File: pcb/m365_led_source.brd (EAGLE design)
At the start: 24 x 69 mm, 36 parts, among them M1 BSC037N08NS5ATMA1, M2 CSD19534Q5A

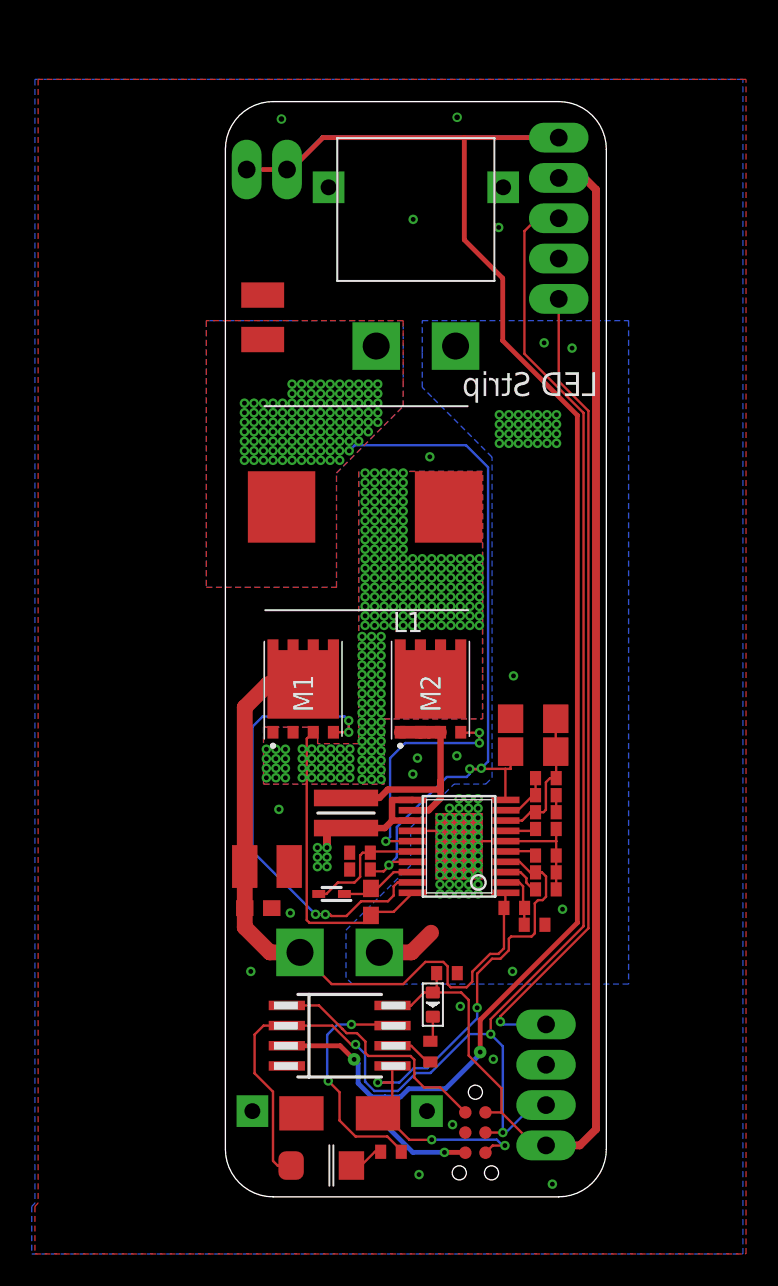
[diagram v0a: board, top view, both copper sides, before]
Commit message: Updated led source board. Added RTC chip + regulator for it Changed the pinout of the attiny45 so that it can be programmed in place
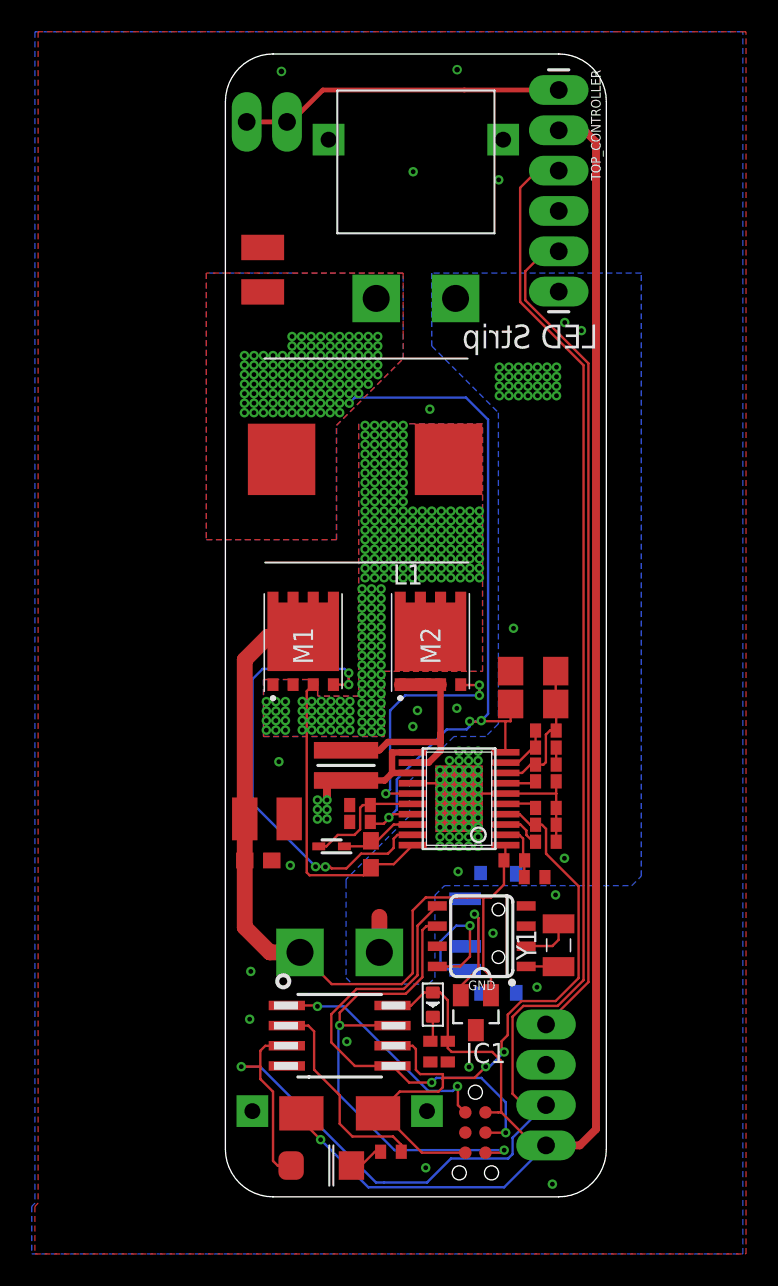
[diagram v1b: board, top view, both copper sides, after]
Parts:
- added GND: DS1307Z, SparkFun-Clocks:SO08-0.15
- added IC1: ZXTR2105FQ, linear:SOT23
- added U$2: MSK-12C02_SMD_SPDT_SWITCH, MSK-12C02 SMD Micro Slider Switch SPDT:MSK-12C02
- added Y1: SMD-3215_2P32.768KHZ12.5PF10PP, SMD-3215_2P32.768KHZ12.5PF10PP:SMD3215_2P32768KHZ125PF10PPM
- TOP_CONTROLLER: device SparkFun-Connectors:1X05_LONGPADS -> SparkFun-Connectors:1X06_LONGPADS
- moved C1 4.94 mm to (14.0, 9.15), turned to 270 degrees
- moved CIN 3.00 mm to (2.62, 23.8)
- moved CINX 3.00 mm to (2.07, 21.2)
- moved C_BOOT 3.00 mm to (9.17, 21.6)
- moved C_COMP 3.00 mm to (20.2, 28.3)
- moved C_COMP2 3.00 mm to (20.2, 29.4)
- moved C_OUT 3.00 mm to (2.35, 58.4)
- moved C_RAMP 3.00 mm to (20.2, 24.5)
- moved C_SS 3.00 mm to (20.2, 26.2)
- moved C_VCC 3.00 mm to (8.48, 24.7)
- moved C_VCCX 3.00 mm to (8.48, 23.6)
- moved D1 3.00 mm to (6.69, 22.1)
- moved L1 3.00 mm to (8.81, 46.5)
- moved LED 3.00 mm to (12.0, 56.6), turned to 270 degrees
- moved LED_DATA 3.00 mm to (3.88, 67.7)
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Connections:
- removed net EN: ATTINY85.5, J2.6, LM5116.4, R_EN_PULLDOWN.2, U$1.P$1
- new net 5V_REG: IC1.2, U$2.COM
- new net N$11: GND.2, Y1.2
- new net N$6: GND.1, Y1.1
- new net PB0: ATTINY85.5, GND.5, J2.4
- new net PB1: ATTINY85.6, J2.5, LM5116.4, R_EN_PULLDOWN.2, U$1.P$1
- new net PB3: ATTINY85.2, R_DATA.1
- net GND: now also GND.3, GND.4, IC1.3, R_LED.1, U$2.GND@1, U$2.GND@2, U$2.GND@3, U$2.GND@4; no longer U$1.P$2
- net M365_5V: now also U$1.P$2
- net M365_DATA: now also ATTINY85.3; no longer ATTINY85.2, J2.4
- net M365_LED_DATA: no longer ATTINY85.3, J2.5
- net N$3: now also GND.8, U$2.L1; no longer ATTINY85.6, R_LED.1
- net PB2: now also GND.6, J2.6; no longer R_DATA.1
- net VIN: now also IC1.1
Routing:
- net M365_LED_DATA: track 124.6 -> 20.5 mm, vias 3 -> 0
- net PB1: track 0.00 -> 42.8 mm, vias 0 -> 2
- net EN: track 38.1 -> 0.00 mm, vias 4 -> 0
- net PB0: track 0.00 -> 29.1 mm, vias 0 -> 2
- net M365_5V: track 85.9 -> 106.0 mm, vias 0 -> 1
- net PB2: track 14.9 -> 31.8 mm
- net PB3: track 0.00 -> 13.2 mm
- net VIN: track 53.3 -> 63.7 mm
- net 5V_REG: track 0.00 -> 8.53 mm, vias 0 -> 1
- net N$3: track 2.80 -> 9.58 mm, vias 0 -> 1
- net M365_DATA: track 97.1 -> 103.5 mm, vias 3 -> 1
- net N$11: track 0.00 -> 3.22 mm
- net N$6: track 0.00 -> 2.05 mm
- net GND: track 27.5 -> 26.2 mm, vias 107 -> 110
- net 42V: track 51.6 -> 52.8 mm, vias 1 -> 0
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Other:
- board size 24 x 69 mm -> 24 x 72 mm
